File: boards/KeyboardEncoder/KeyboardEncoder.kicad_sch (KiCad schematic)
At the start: 21 parts, among them J1 ISP, J2 Encoder, J3 MIDI Out, J4 SelectRX, J5 MIDI In, J7 BoardCon, J8 PistonEncoder, U1 ATmega48-20P, U2 6N138, U3 74LS14

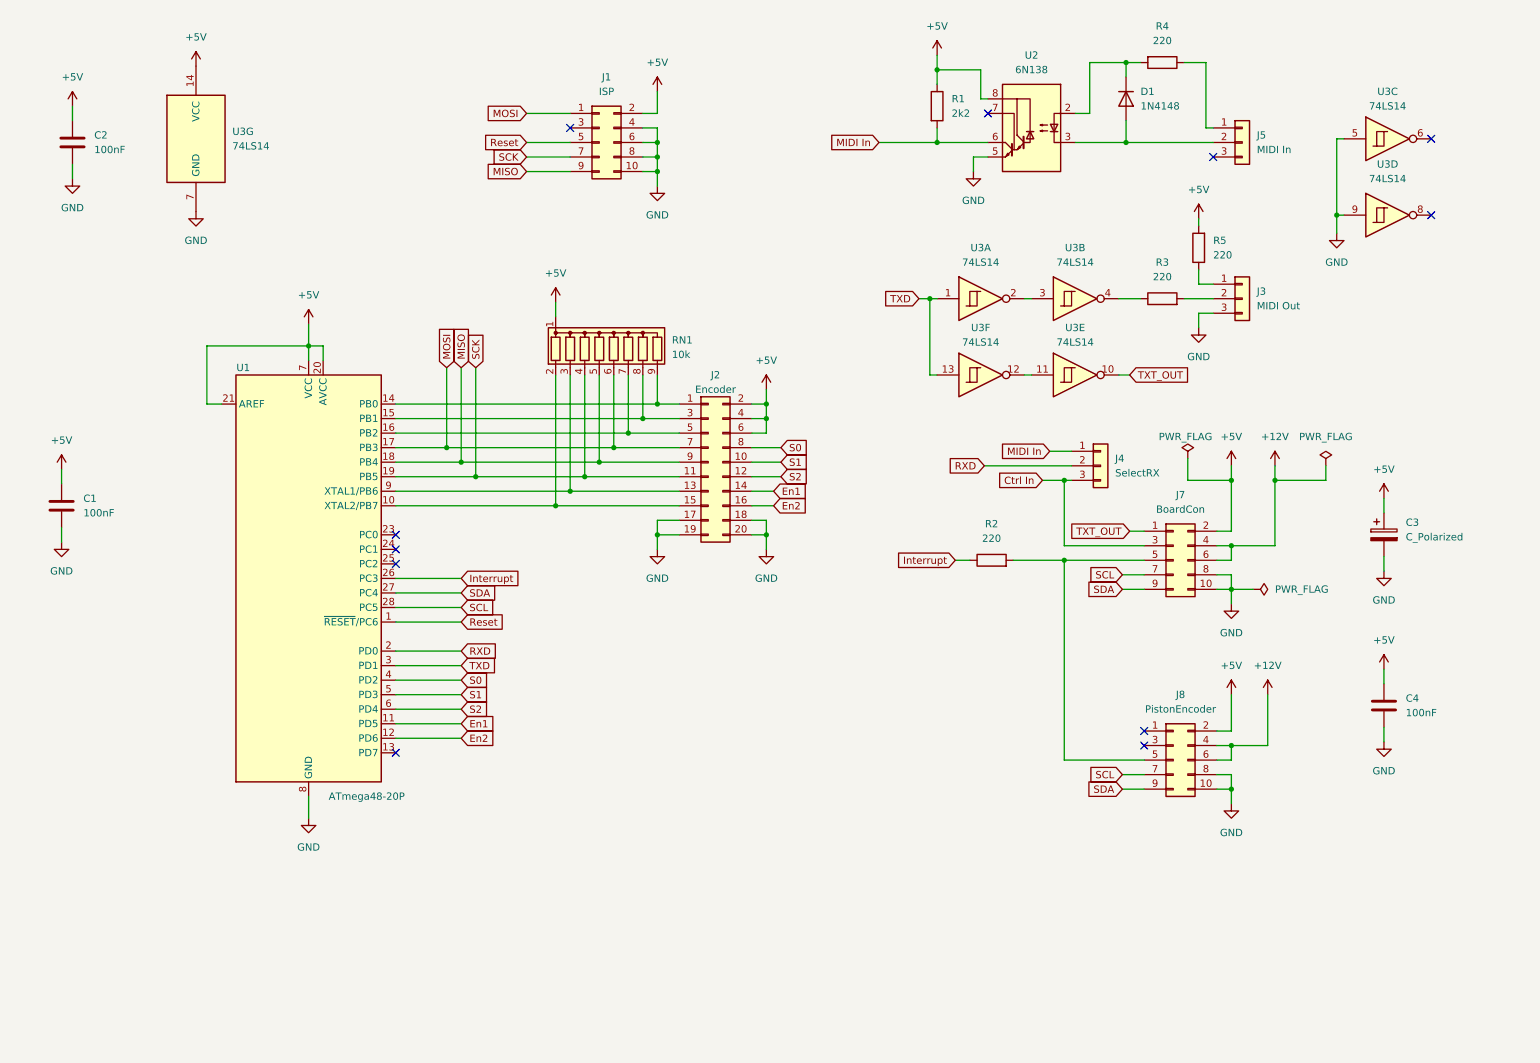
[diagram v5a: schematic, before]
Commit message: Updated to KiCAD 8, fixed optocouplers for MIDI and added powersupplies
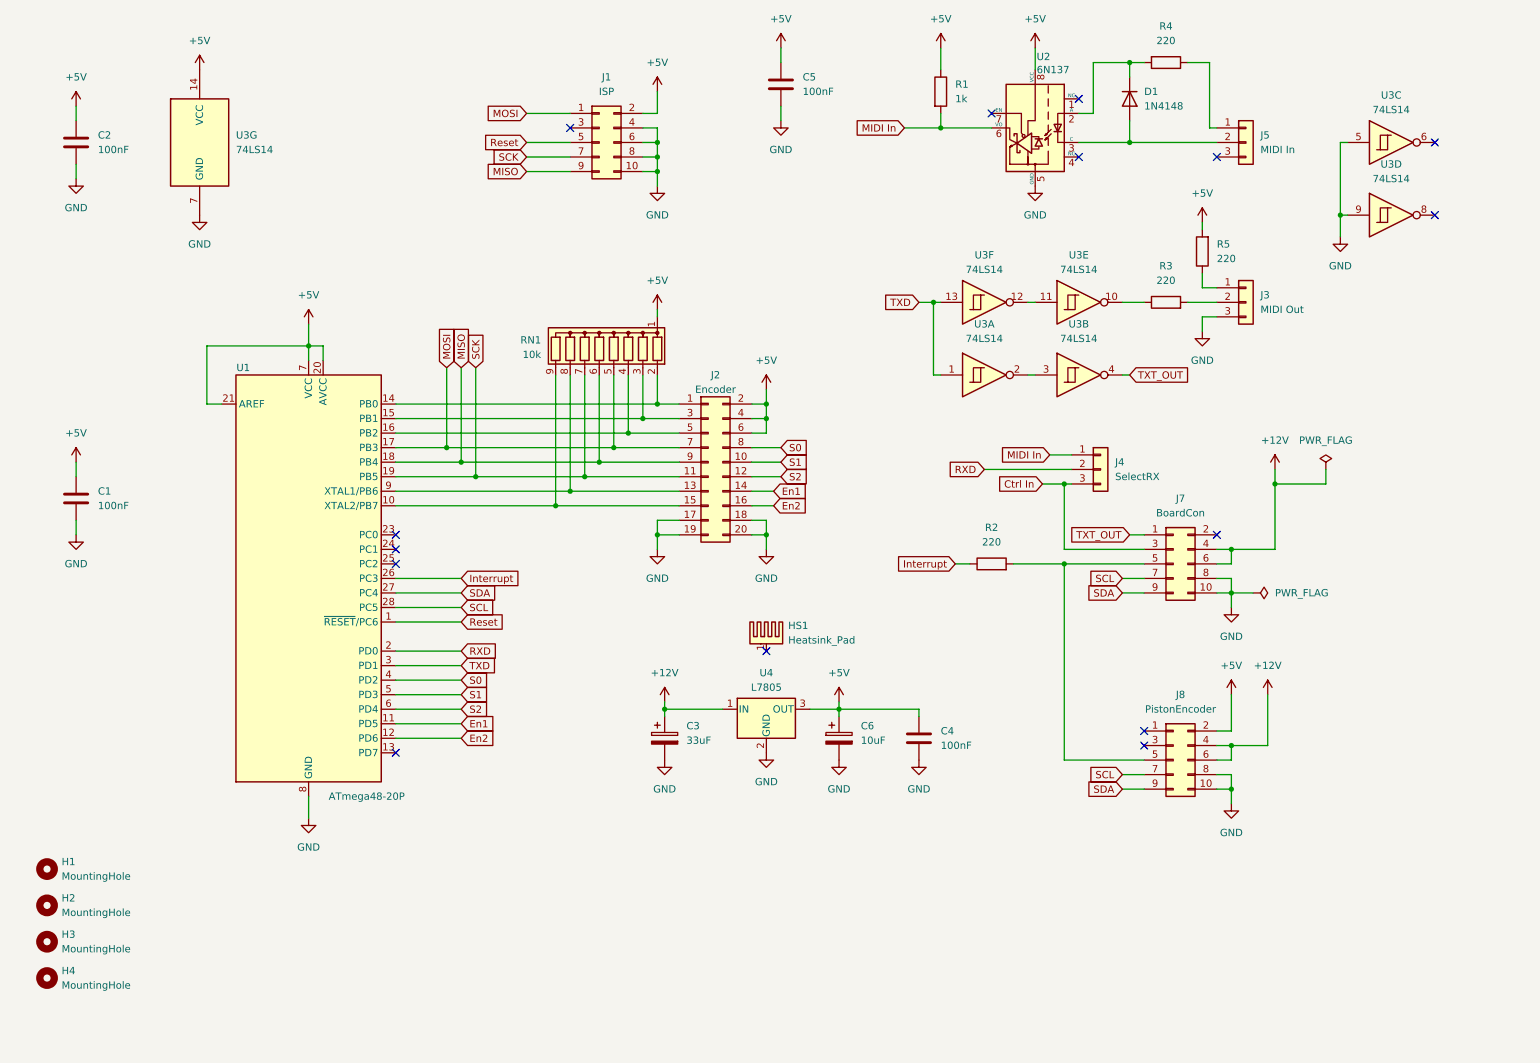
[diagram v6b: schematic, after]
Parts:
- removed U2: 6N138, Package_DIP:DIP-8_W7.62mm, symbol Isolator:6N138
- added C5: 100nF, Capacitor_THT:C_Disc_D4.3mm_W1.9mm_P5.00mm, symbol Device:C
- added C6: 10uF, Capacitor_THT:CP_Radial_D6.3mm_P2.50mm, symbol Device:C_Polarized
- added H1, H2, H3, H4: MountingHole, MountingHole:MountingHole_3.2mm_M3, symbol Mechanical:MountingHole
- added HS1: Heatsink_Pad, Heatsink:Heatsink_AAVID_576802B03900G, symbol Mechanical:Heatsink_Pad
- added U2: 6N137, Package_DIP:DIP-8_W7.62mm, symbol Isolator:6N137
- added U4: L7805, Package_TO_SOT_THT:TO-220-3_Vertical, symbol Regulator_Linear:L7805
- C3: value C_Polarized -> 33uF; footprint Capacitor_THT:CP_Radial_D10.0mm_P5.00mm -> Capacitor_THT:CP_Radial_D7.5mm_P2.50mm
- J1, J7: footprint Connector_IDC:IDC-Header_2x05_P2.54mm_Vertical -> Connector_IDC:IDC-Header_2x05_P2.54mm_Horizontal
- J2: footprint Connector_IDC:IDC-Header_2x10_P2.54mm_Vertical -> Connector_IDC:IDC-Header_2x10_P2.54mm_Horizontal
- R1: value 2k2 -> 1k
- R2, R3, R4, R5: footprint Resistor_THT:R_Axial_DIN0204_L3.6mm_D1.6mm_P2.54mm_Vertical -> Resistor_THT:R_Axial_DIN0204_L3.6mm_D1.6mm_P7.62mm_Horizontal
- U3: footprint (none) -> Package_DIP:DIP-14_W7.62mm
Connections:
- net +12V: now also C3.1, U4.1 (IN)
- net +5V: now also C5.1, C6.1, U2.8 (VCC), U4.3 (OUT); no longer C3.1, J7.2 (Pin_2)
- net GND: now also C5.2, C6.2, U2.5 (GND), U4.2 (GND)
- net MIDI In: now also U2.6 (VO)
- net MISO: now also RN1.6 (R5); no longer RN1.5 (R4)
- net MOSI: now also RN1.5 (R4); no longer RN1.6 (R5)
- net SCK: now also RN1.7 (R6); no longer RN1.4 (R3)
- net TXT_OUT: now also U3.4; no longer U3.10
- net at J2.15 (Pin_15), U1.10 (XTAL2/PB7): now also RN1.9 (R8); no longer RN1.2 (R1)
- net at J2.1 (Pin_1), U1.14 (PB0): now also RN1.2 (R1); no longer RN1.9 (R8)
- net at J2.3 (Pin_3), U1.15 (PB1): now also RN1.3 (R2); no longer RN1.8 (R7)
- net at J2.5 (Pin_5), U1.16 (PB2): now also RN1.4 (R3); no longer RN1.7 (R6)
- net at J2.13 (Pin_13), U1.9 (XTAL1/PB6): now also RN1.8 (R7); no longer RN1.3 (R2)
- net at R3.1: now also U3.10; no longer U3.4
- net at D1.2 (A), J5.2 (Pin_2): now also U2.3 (C)
- net at D1.1 (K), R4.2: now also U2.2 (A)
- no-connect marks 11 -> 15
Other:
- moved on the sheet: C1, C2, C3, C4, D1, J3, J4, J5, J7, R1, R2, R3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

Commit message: Using custom TO220 cooler, fixed and finished several PCBs
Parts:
- HS1: footprint Heatsink:Heatsink_AAVID_576802B03900G -> Custom_Heatsinks:Heatsink_Aavid_TO-220_H12.7mm
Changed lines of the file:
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@@
 			)
 		)
-		(property "Footprint" "Heatsink:Heatsink_AAVID_576802B03900G"
+		(property "Footprint" "Custom_Heatsinks:Heatsink_Aavid_TO-220_H12.7mm"
 			(at 153.9748 125.73 0)
 			(effects

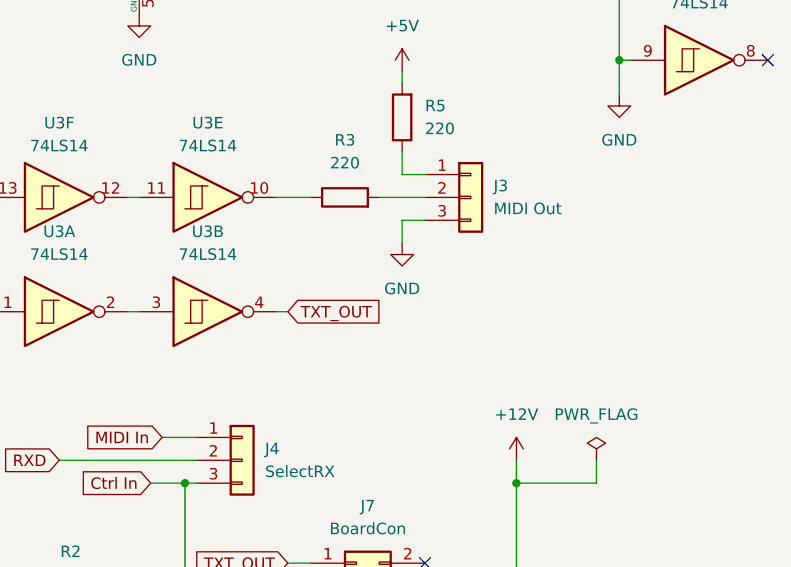
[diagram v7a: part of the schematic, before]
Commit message: Added Optocoupler and RS232 converter to UART board lines.
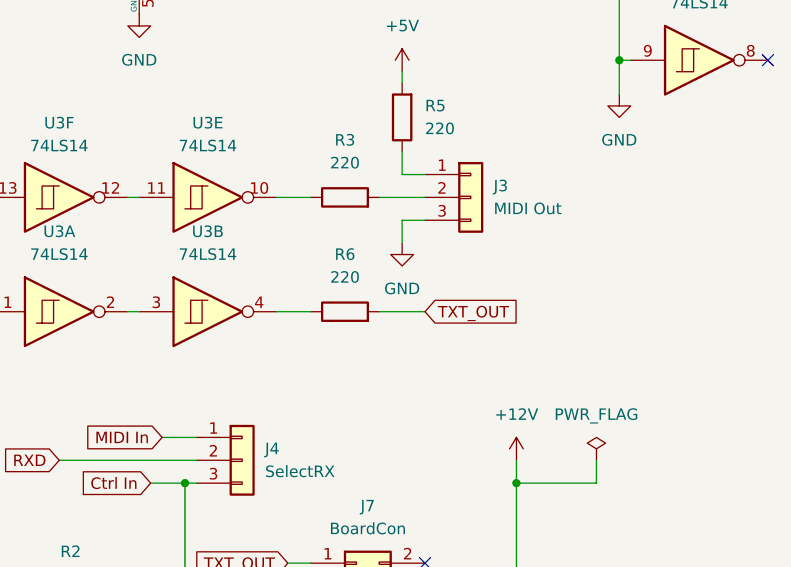
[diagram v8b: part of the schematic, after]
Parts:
- added R6: 220, Resistor_THT:R_Axial_DIN0204_L3.6mm_D1.6mm_P7.62mm_Horizontal, symbol Device:R
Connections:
- net TXT_OUT: now also R6.2; no longer U3.4
- new net: R6.1, U3.4
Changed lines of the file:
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@@
+	(wire
+		(pts
+			(xy 215.9 78.74) (xy 219.71 78.74)
+		)
+		(stroke
+			(width 0)
+			(type default)
+		)
+	)
 	(wire
 		(pts
@@
 	(wire
 		(pts
+			(xy 227.33 78.74) (xy 232.41 78.74)
+		)
+		(stroke
+			(width 0)
+			(type default)
+		)
+	)
+	(wire
+		(pts
 			(xy 210.82 33.02) (xy 210.82 24.13)
 		)
@@
 	(wire
 		(pts
-			(xy 217.17 78.74) (xy 215.9 78.74)
-		)
-		(stroke
-			(width 0)
-			(type default)
-		)
-	)
-	(wire
-		(pts
 			(xy 205.74 109.22) (xy 219.71 109.22)
 		)
@@
 	(global_label "TXT_OUT"
 		(shape input)
-		(at 217.17 78.74 0)
+		(at 232.41 78.74 0)
 		(fields_autoplaced yes)
 		(effects
@@
 		)
 		(property "Intersheetrefs" "${INTERSHEET_REFS}"
-			(at 227.8961 78.74 0)
+			(at 243.1361 78.74 0)
 			(effects
 				(font
@@
 					(unit 1)
 				)
+			)
+		)
+	)
+	(symbol
+		(lib_id "Device:R")
+		(at 223.52 78.74 90)
+		(unit 1)
+		(exclude_from_sim no)
+		(in_bom yes)
+		(on_board yes)
+		(dnp no)
+		(fields_autoplaced yes)
+		(property "Reference" "R6"
+			(at 223.52 72.39 90)
+			(effects
+				(font
+					(size 1.27 1.27)
+				)
+			)
+		)
+		(property "Value" "220"
+			(at 223.52 74.93 90)
+			(effects
+				(font
+					(size 1.27 1.27)
+				)
+			)
+		)
+		(property "Footprint" "Resistor_THT:R_Axial_DIN0204_L3.6mm_D1.6mm_P7.62mm_Horizontal"
+			(at 223.52 80.518 90)
+			(effects
+				(font
+					(size 1.27 1.27)
+				)
+				(hide yes)
+			)
+		)
+		(property "Datasheet" "~"
+			(at 223.52 78.74 0)
+			(effects
+				(font
+					(size 1.27 1.27)
+				)
+				(hide yes)
+			)
+		)
+		(property "Description" "Resistor"
+			(at 223.52 78.74 0)
+			(effects
+				(font
+					(size 1.27 1.27)
+				)
+				(hide yes)
+			)
+		)
+		(pin "1"
+		)
+		(pin "2"
+		)
+		(instances
+			(project "KeyboardEncoder"
+				(path "/203cfae3-c134-4f8b-b17f-2675fc7b8ec3"
+					(reference "R6")
+					(unit 1)
+				)
